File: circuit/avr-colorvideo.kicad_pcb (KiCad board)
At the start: 2 copper layers, 229.9 x 111.8 mm, 148 parts, among them J1 USB-B, J2 AVR-ISP-6, J3 RCA, J4 RCA, J5 SPI1, J6 SPI0, J7 ANALOG, J8 6P6C, J9 6P6C, K1 SW_Push, K10 SW_Push, K11 SW_Push, K12 SW_Push, K13 SW_Push, K14 SW_Push, K15 SW_Push, K16 SW_Push, K17 SW_Push, K18 SW_Push, K19 SW_Push, K2 SW_Push, K20 SW_Push, K21 SW_Push, K22 SW_Push, K23 SW_Push, K24 SW_Push, K25 SW_Push, K26 SW_Push, K27 SW_Push, K28 SW_Push, K29 SW_Push, K3 SW_Push, K30 SW_Push, K31 SW_Push, K32 SW_Push, K33 SW_Push, K34 SW_Push, K35 SW_Push, K36 SW_Push, K37 SW_Push, K38 SW_Push, K39 SW_Push, K4 SW_Push, K40 SW_Push, K41 SW_Push, K42 SW_Push, K43 SW_Push, K44 SW_Push, K45 SW_Push, K46 SW_Push, K47 SW_Push, K5 SW_Push, K6 SW_Push, K7 SW_Push, K8 SW_Push, K9 SW_Push, SW1 SW_Push, SW2 SPI1/ISP, U1 ATmega1284P-PU, U2 74HC157, U3 74HC157, U4 74HC166, U5 74HC166, U6 FT230XS, Y1 14.31818MHz

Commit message: WIP: BOM and schematic edits
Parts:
- C1, C10, C11, C12, C13, C14, C15, C16, C2, C3, C4, C5, C7, C8, C9: footprint Capacitor_SMD:C_0603_1608Metric_Pad1.05x0.95mm_HandSolder -> Capacitor_SMD:C_0805_2012Metric_Pad1.15x1.40mm_HandSolder
- R5: footprint Resistor_SMD:R_1206_3216Metric -> Resistor_SMD:R_0805_2012Metric
- moved C11 1.43 mm to (102.6, 42.3)

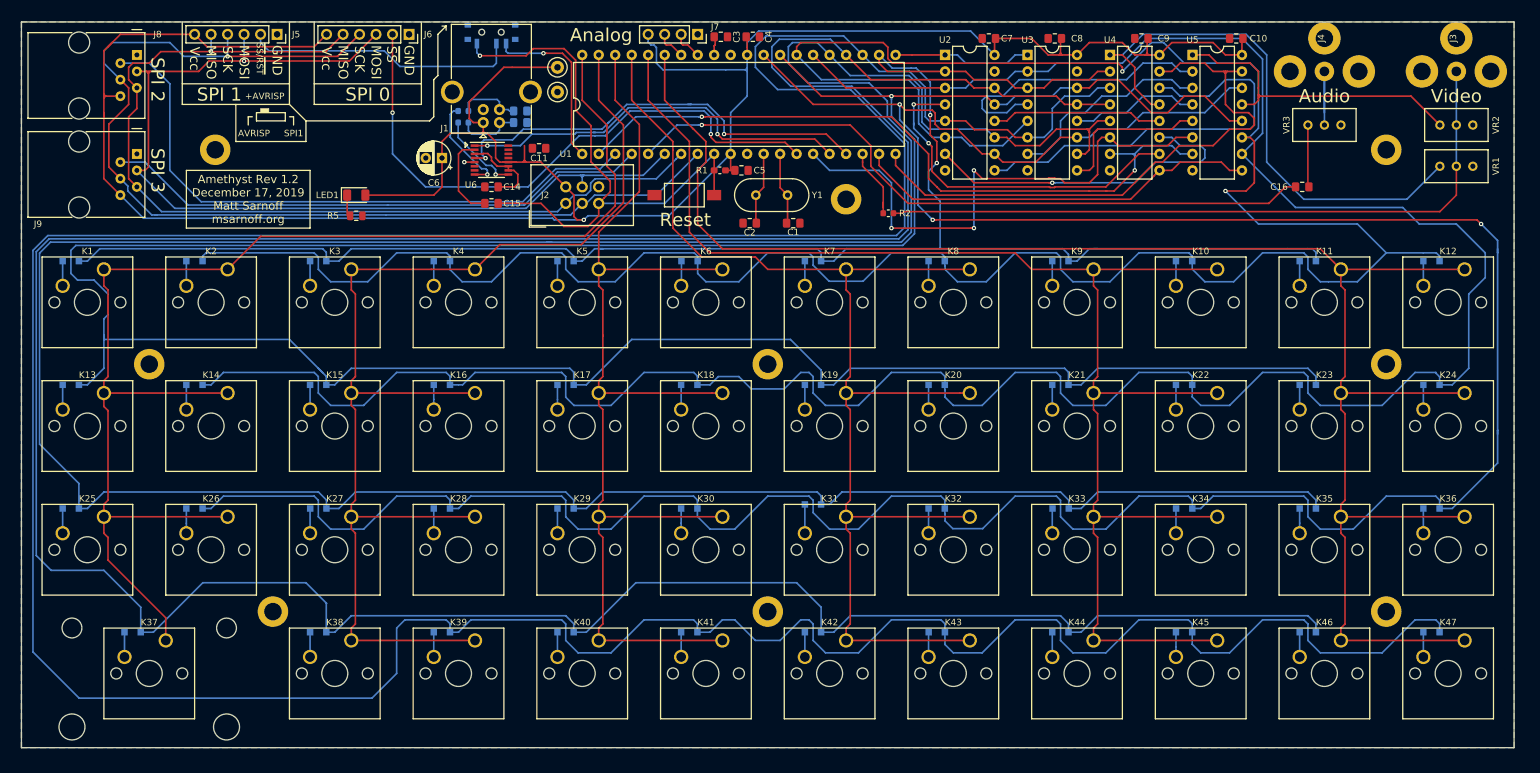
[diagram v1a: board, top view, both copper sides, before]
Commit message: WIP: rerouting traces
accommodating larger 0805 parts

fixing DRC
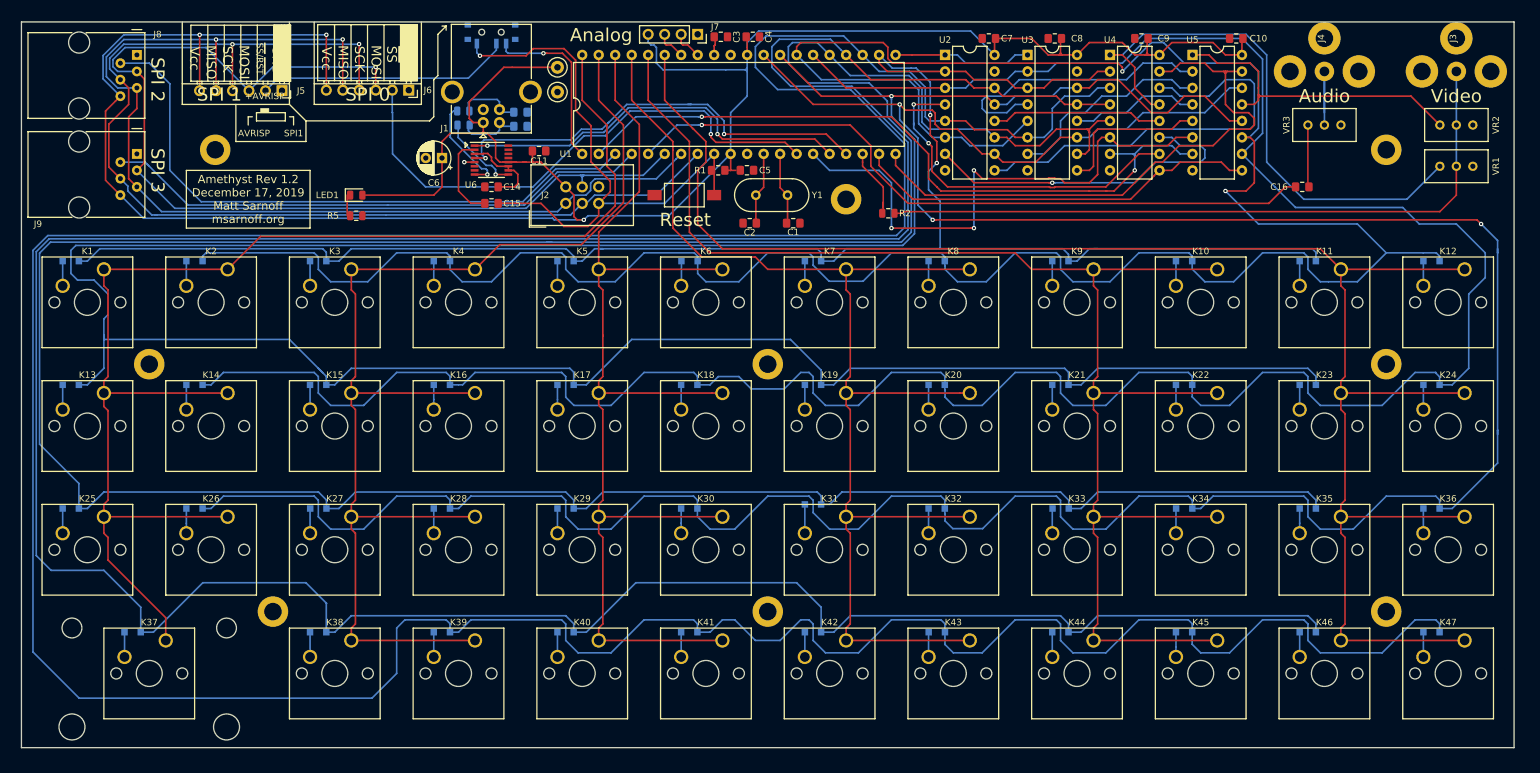
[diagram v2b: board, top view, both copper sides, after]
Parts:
- J5, J6: footprint Connector_PinSocket_2.54mm:PinSocket_1x06_P2.54mm_Vertical -> Connector_PinSocket_2.54mm:PinSocket_1x06_P2.54mm_Horizontal
- LED1: footprint LED_SMD:LED_1206_3216Metric -> LED_SMD:LED_0805_2012Metric
- R1: footprint Resistor_SMD:R_0603_1608Metric_Pad1.05x0.95mm_HandSolder -> Resistor_SMD:R_0805_2012Metric_Pad1.15x1.40mm_HandSolder
- R2, R3, R4: footprint Resistor_SMD:R_0603_1608Metric -> Resistor_SMD:R_0805_2012Metric
- moved J5 8.72 mm to (63.0, 33.5)
- moved J6 8.61 mm to (82.5, 33.4)
- moved C5 0.85 mm to (134.6, 45.7)
- moved C12 0.58 mm to (99.7, 38.9)
- moved C11 0.42 mm to (102.6, 42.7)
- moved R3 0.39 mm to (91.0, 38.7)
- moved R1 0.25 mm to (130.2, 45.7)
- moved C13 0.19 mm to (99.7, 36.8)
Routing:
- net /MISO: track 147.5 -> 167.7 mm, vias 1 -> 2
- net VCC: track 383.8 -> 394.7 mm, vias 1 -> 3
- net /MOSI: track 150.4 -> 160.0 mm
- net /~SS0: track 92.1 -> 83.6 mm, vias 2 -> 1
- net /SCK: track 164.6 -> 171.1 mm, vias 1 -> 2
- net Net-(J5-Pad2): track 42.3 -> 39.1 mm
- removed copper zone on B.Cu, net GND
- removed copper zone on F.Cu, net GND

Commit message: Refill copper pours
- Pass DRC except for known issue:
  https://bugs.launchpad.net/kicad/+bug/1831776
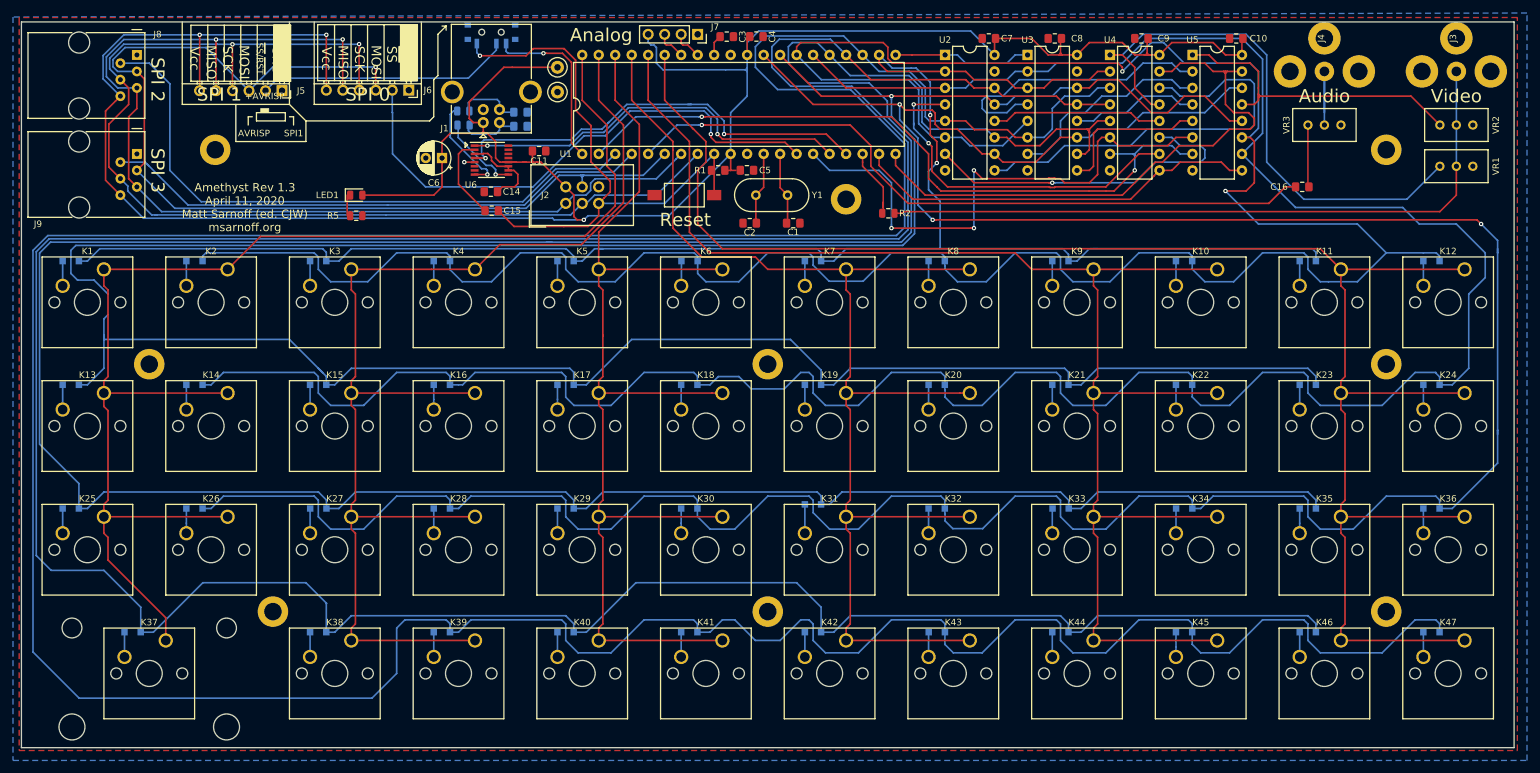
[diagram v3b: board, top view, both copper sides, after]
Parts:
- moved C15 1.13 mm to (95.3, 51.9)
- moved C3 0.91 mm to (131.5, 25.1)
- moved C14 0.75 mm to (95.2, 49.0)
- moved C4 0.56 mm to (136.1, 25.1)
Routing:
- net /~RESET: track 90.0 -> 89.4 mm
- added copper zone on B.Cu, net GND
- added copper zone on F.Cu, net GND
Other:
- board text added: "Amethyst Rev 1.3 April 11, 2020 Matt Sarnoff (ed. CJW) msarnoff.org"
- board text removed: "Amethyst Rev 1.2 December 17, 2019 Matt Sarnoff msarnoff.org"
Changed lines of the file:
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@@
   (general
     (thickness 1.6)
-    (drawings 107)
-    (tracks 1491)
+    (drawings 103)
+    (tracks 1490)
     (zones 0)
     (modules 148)
@@
     (34 B.Paste user)
     (35 F.Paste user)
-    (36 B.SilkS user hide)
-    (37 F.SilkS user hide)
+    (36 B.SilkS user)
+    (37 F.SilkS user)
     (38 B.Mask user)
     (39 F.Mask user)
@@
     (44 Edge.Cuts user)
     (45 Margin user)
-    (46 B.CrtYd user hide)
+    (46 B.CrtYd user)
     (47 F.CrtYd user)
-    (48 B.Fab user hide)
-    (49 F.Fab user hide)
+    (48 B.Fab user)
+    (49 F.Fab user)
   )
   (setup
@@
   )
   (module Capacitor_SMD:C_0805_2012Metric_Pad1.15x1.40mm_HandSolder (layer F.Cu)
-    (at 95.25 48.26 180)
+    (at 95.16 49 180)
     (descr "Capacitor SMD 0805 (2012 Metric), square (rectangular) end terminal, IPC_7351 nominal with elongated pad for handsoldering. (Body size source: https://docs.google.com/spreadsheets/d/1BsfQQcO9C6DZCsRaXUlFlo91Tg2WpOkGARC1WS5S8t0/edit?usp=sharing), generated with kicad-footprint-generator")
     (tags "capacitor handsolder")
@@
   )
   (module Capacitor_SMD:C_0805_2012Metric_Pad1.15x1.40mm_HandSolder (layer F.Cu)
-    (at 130.57 25.146)
+    (at 131.48 25.12)
     (descr "Capacitor SMD 0805 (2012 Metric), square (rectangular) end terminal, IPC_7351 nominal with elongated pad for handsoldering. (Body size source: https://docs.google.com/spreadsheets/d/1BsfQQcO9C6DZCsRaXUlFlo91Tg2WpOkGARC1WS5S8t0/edit?usp=sharing), generated with kicad-footprint-generator")
     (tags "capacitor handsolder")
@@
   )
   (module Capacitor_SMD:C_0805_2012Metric_Pad1.15x1.40mm_HandSolder (layer F.Cu)
-    (at 135.495 25.146)
+    (at 136.05 25.11)
     (descr "Capacitor SMD 0805 (2012 Metric), square (rectangular) end terminal, IPC_7351 nominal with elongated pad for handsoldering. (Body size source: https://docs.google.com/spreadsheets/d/1BsfQQcO9C6DZCsRaXUlFlo91Tg2WpOkGARC1WS5S8t0/edit?usp=sharing), generated with kicad-footprint-generator")
     (tags "capacitor handsolder")
@@
   )
   (module Capacitor_SMD:C_0805_2012Metric_Pad1.15x1.40mm_HandSolder (layer F.Cu)
-    (at 95.25 50.8 180)
+    (at 95.28 51.93 180)
     (descr "Capacitor SMD 0805 (2012 Metric), square (rectangular) end terminal, IPC_7351 nominal with elongated pad for handsoldering. (Body size source: https://docs.google.com/spreadsheets/d/1BsfQQcO9C6DZCsRaXUlFlo91Tg2WpOkGARC1WS5S8t0/edit?usp=sharing), generated with kicad-footprint-generator")
     (tags "capacitor handsolder")
@@
   (gr_line (start 84.455 35.56) (end 67.945 35.56) (layer F.SilkS) (width 0.15))
   (gr_line (start 84.455 22.86) (end 84.455 35.56) (layer F.SilkS) (width 0.15))
-  (gr_line (start 48.26 54.61) (end 48.26 45.72) (layer F.SilkS) (width 0.15))
-  (gr_line (start 67.31 54.61) (end 48.26 54.61) (layer F.SilkS) (width 0.15))
-  (gr_line (start 67.31 45.72) (end 67.31 54.61) (layer F.SilkS) (width 0.15))
-  (gr_line (start 48.26 45.72) (end 67.31 45.72) (layer F.SilkS) (width 0.15))
-  (gr_text "Amethyst Rev 1.2\nDecember 17, 2019\nMatt Sarnoff\nmsarnoff.org" (at 57.785 50.165) (layer F.SilkS)
+  (gr_text "Amethyst Rev 1.3\nApril 11, 2020\nMatt Sarnoff (ed. CJW)\nmsarnoff.org" (at 57.27 51.42) (layer F.SilkS)
     (effects (font (size 1.27 1.27) (thickness 0.15)))
   )
@@
   (segment (start 134.62 30.48) (end 134.62 34.29) (width 0.254) (layer B.Cu) (net 4))
   (segment (start 134.62 30.226) (end 134.62 30.48) (width 0.254) (layer B.Cu) (net 4))
-  (segment (start 134.62 26.80863) (end 134.62 25.146) (width 0.254) (layer F.Cu) (net 4))
-  (segment (start 134.62 27.94) (end 134.62 26.80863) (width 0.254) (layer F.Cu) (net 4))
   (segment (start 131.318 30.226) (end 134.366 30.226) (width 0.254) (layer B.Cu) (net 4))
   (segment (start 121.666 30.226) (end 131.318 30.226) (width 0.254) (layer B.Cu) (net 4))
@@
   (segment (start 100.584 44.45) (end 101.63 44.45) (width 0.254) (layer F.Cu) (net 4))
   (segment (start 101.63 44.45) (end 102.235 44.45) (width 0.254) (layer F.Cu) (net 4))
+  (segment (start 134.62 25.515) (end 135.025 25.11) (width 0.254) (layer F.Cu) (net 4))
+  (segment (start 134.62 27.94) (end 134.62 25.515) (width 0.254) (layer F.Cu) (net 4))
   (segment (start 106.68 50.8) (end 107.95 49.53) (width 0.254) (layer B.Cu) (net 5))
   (segment (start 123.660001 43.979999) (end 124.46 43.18) (width 0.254) (layer B.Cu) (net 5))
@@
   (segment (start 106.3879 54.356) (end 110.109 54.356) (width 0.254) (layer F.Cu) (net 8))
   (segment (start 106.3879 54.356) (end 106.3879 54.3179) (width 0.254) (layer F.Cu) (net 8))
-  (segment (start 96.125 50.8) (end 102.87 50.8) (width 0.254) (layer F.Cu) (net 8))
-  (segment (start 106.3879 54.3179) (end 102.87 50.8) (width 0.254) (layer F.Cu) (net 8))
   (segment (start 111.76 50.8) (end 112.623599 49.936401) (width 0.254) (layer F.Cu) (net 8))
   (segment (start 112.623599 49.936401) (end 113.538 49.022) (width 0.254) (layer F.Cu) (net 8))
@@
   (segment (start 100.584 28.067) (end 101.688907 26.962093) (width 0.254) (layer F.Cu) (net 8))
   (segment (start 108.204 28.745566) (end 106.467717 27.009283) (width 0.254) (layer F.Cu) (net 8))
+  (segment (start 98.731 54.356) (end 96.305 51.93) (width 0.254) (layer F.Cu) (net 8))
+  (segment (start 106.3879 54.356) (end 98.731 54.356) (width 0.254) (layer F.Cu) (net 8))
   (segment (start 243.84 38.735) (end 243.84 30.48) (width 0.254) (layer B.Cu) (net 9))
   (segment (start 243.84 45.085) (end 243.84 38.735) (width 0.254) (layer B.Cu) (net 9))
@@
   (segment (start 157.15 52.324) (end 158.496 52.324) (width 0.254) (layer F.Cu) (net 9))
   (segment (start 158.75 52.07) (end 241.3 52.07) (width 0.254) (layer F.Cu) (net 9))
-  (segment (start 129.695 25.146) (end 129.695 26.388) (width 0.254) (layer F.Cu) (net 10))
-  (segment (start 129.54 26.543) (end 129.54 27.94) (width 0.254) (layer F.Cu) (net 10))
-  (segment (start 129.695 26.388) (end 129.54 26.543) (width 0.254) (layer F.Cu) (net 10))
+  (segment (start 129.54 26.035) (end 130.455 25.12) (width 0.254) (layer F.Cu) (net 10))
+  (segment (start 129.54 27.94) (end 129.54 26.035) (width 0.254) (layer F.Cu) (net 10))
   (segment (start 152.4 45.085) (end 152.4 44.45) (width 0.254) (layer F.Cu) (net 11))
   (segment (start 155.575 48.26) (end 152.4 45.085) (width 0.254) (layer F.Cu) (net 11))
@@
   (segment (start 98.806 48.26) (end 99.314 47.752) (width 0.254) (layer F.Cu) (net 111))
   (segment (start 99.314 47.752) (end 99.314 46.33) (width 0.254) (layer F.Cu) (net 111))
-  (segment (start 96.125 48.26) (end 98.806 48.26) (width 0.254) (layer F.Cu) (net 111))
   (segment (start 95.25 43.688) (end 95.25 44.196) (width 0.254) (layer F.Cu) (net 111))
   (segment (start 94.680786 43.118786) (end 95.25 43.688) (width 0.254) (layer F.Cu) (net 111))
@@
   (segment (start 95.25 44.196) (end 96.139 45.085) (width 0.254) (layer F.Cu) (net 111))
   (segment (start 92.65 43.18) (end 93.924626 43.18) (width 0.254) (layer F.Cu) (net 111))
+  (segment (start 96.925 48.26) (end 96.185 49) (width 0.254) (layer F.Cu) (net 111))
+  (segment (start 98.806 48.26) (end 96.925 48.26) (width 0.254) (layer F.Cu) (net 111))
   (segment (start 90.805 42.545) (end 92.65 42.545) (width 0.254) (layer F.Cu) (net 112))
   (segment (start 90.17 43.18) (end 90.805 42.545) (width 0.254) (layer F.Cu) (net 112))
-  (segment (start 92.075 50.8) (end 90.17 48.895) (width 0.254) (layer F.Cu) (net 112))
-  (segment (start 90.17 48.895) (end 90.17 43.18) (width 0.254) (layer F.Cu) (net 112))
-  (segment (start 94.375 50.8) (end 92.075 50.8) (width 0.254) (layer F.Cu) (net 112))
+  (segment (start 90.17 47.845) (end 94.255 51.93) (width 0.254) (layer F.Cu) (net 112))
+  (segment (start 90.17 43.18) (end 90.17 47.845) (width 0.254) (layer F.Cu) (net 112))
   (segment (start 61.299999 32.600001) (end 60.45 33.45) (width 0.254) (layer B.Cu) (net 113))
   (segment (start 62.387001 31.512999) (end 61.299999 32.600001) (width 0.254) (layer B.Cu) (net 113))
@@
   (segment (start 96 27.199) (end 91.686001 31.512999) (width 0.254) (layer B.Cu) (net 113))
   (segment (start 96 26.195) (end 96 27.199) (width 0.254) (layer B.Cu) (net 113))
+  (zone (net 2) (net_name GND) (layer F.Cu) (hatch edge 0.508)
+    (connect_pads (clearance 0.254))
+    (min_thickness 0.254)
+    (fill yes (arc_segments 32) (thermal_gap 0.508) (thermal_bridge_width 0.508))
+    (polygon
+      (pts
+        (xy 22.51 22.48) (xy 22.51 135.06) (xy 253.23 135.06) (xy 253.23 22.18) (xy 22.51 22.18)
+      )
+    )
+  )
+  (zone (net 2) (net_name GND) (layer B.Cu) (hatch edge 0.508)
+    (connect_pads (clearance 0.254))
+    (min_thickness 0.254)
+    (fill yes (arc_segments 32) (thermal_gap 0.508) (thermal_bridge_width 0.508))
+    (polygon
+      (pts
+        (xy 21.56 22.1) (xy 21.56 136.59) (xy 254.72 136.59) (xy 254.72 21.48)
+      )
+    )
+  )
 )
